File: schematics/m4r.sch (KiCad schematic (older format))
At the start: 88 parts, among them IC10 SN74LVC1G0832, IC11 MAX-M8Q, IC12 NC7SZ04, IC13 CS2100-CP, IC14 Si4463, IC15 NCP380, IC16 Si53307, IC17 BGM1043N7, IC18 ADL5324, IC7 NCP4620, IC8 MCP2562, IC9 STM32F405RxTx, P3 SWD_TC, Y3 TCXO

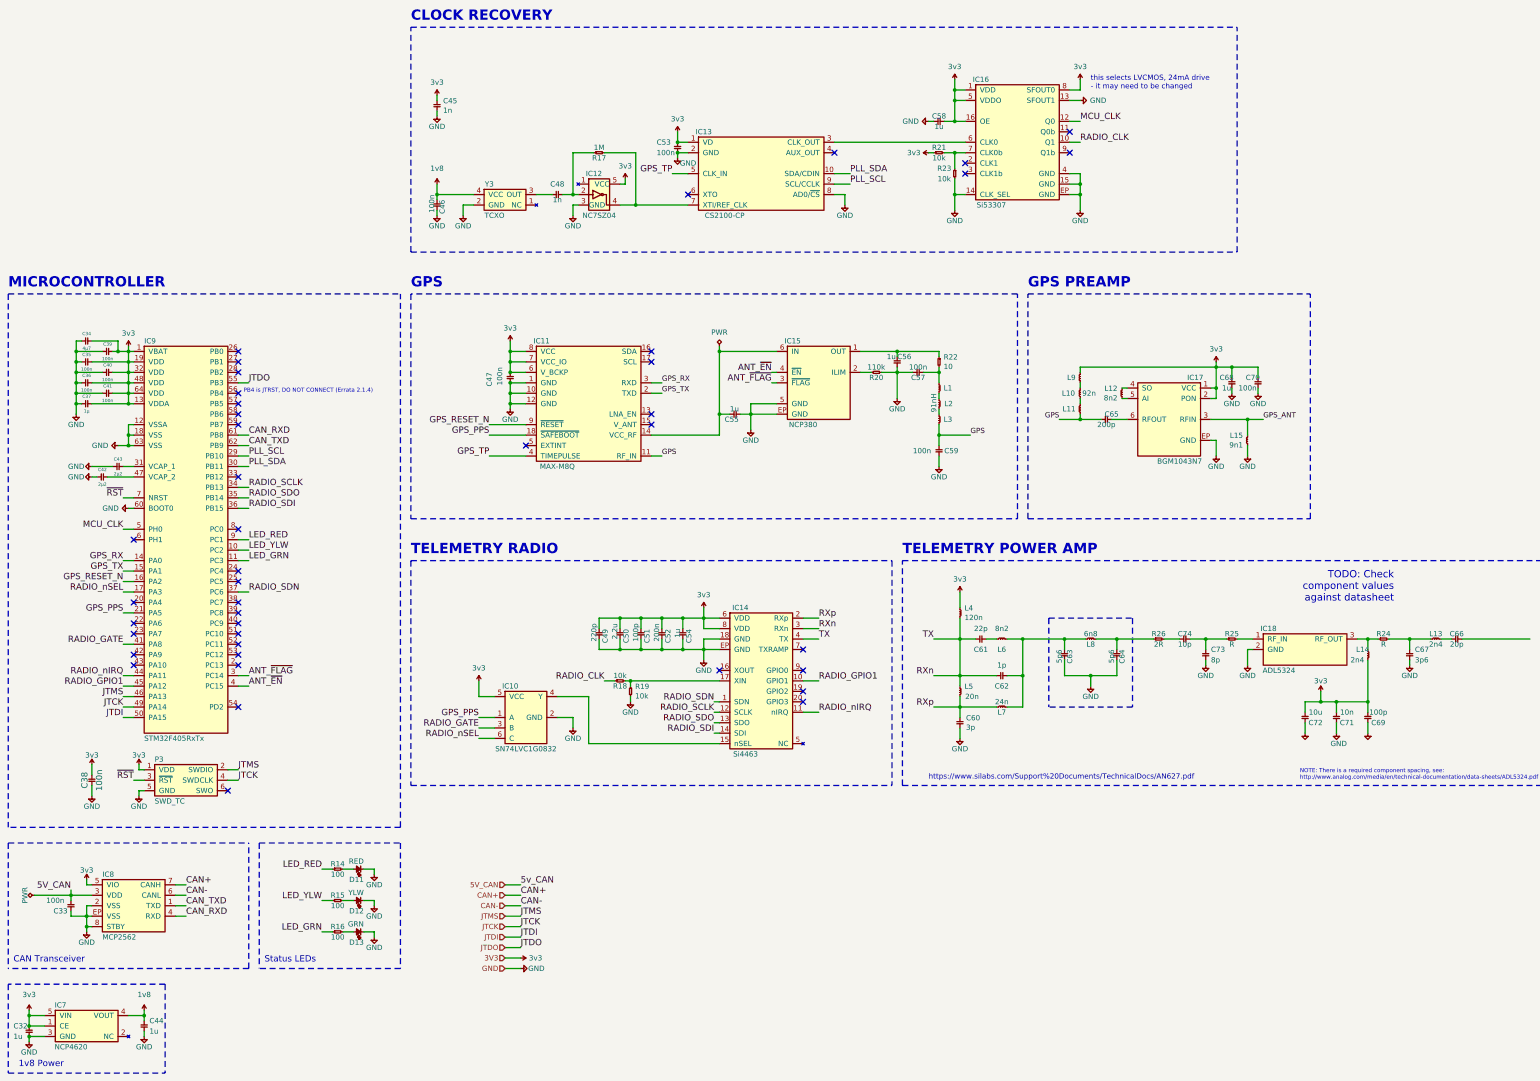
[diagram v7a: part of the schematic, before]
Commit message: Normalise all font sizes to 50 mil
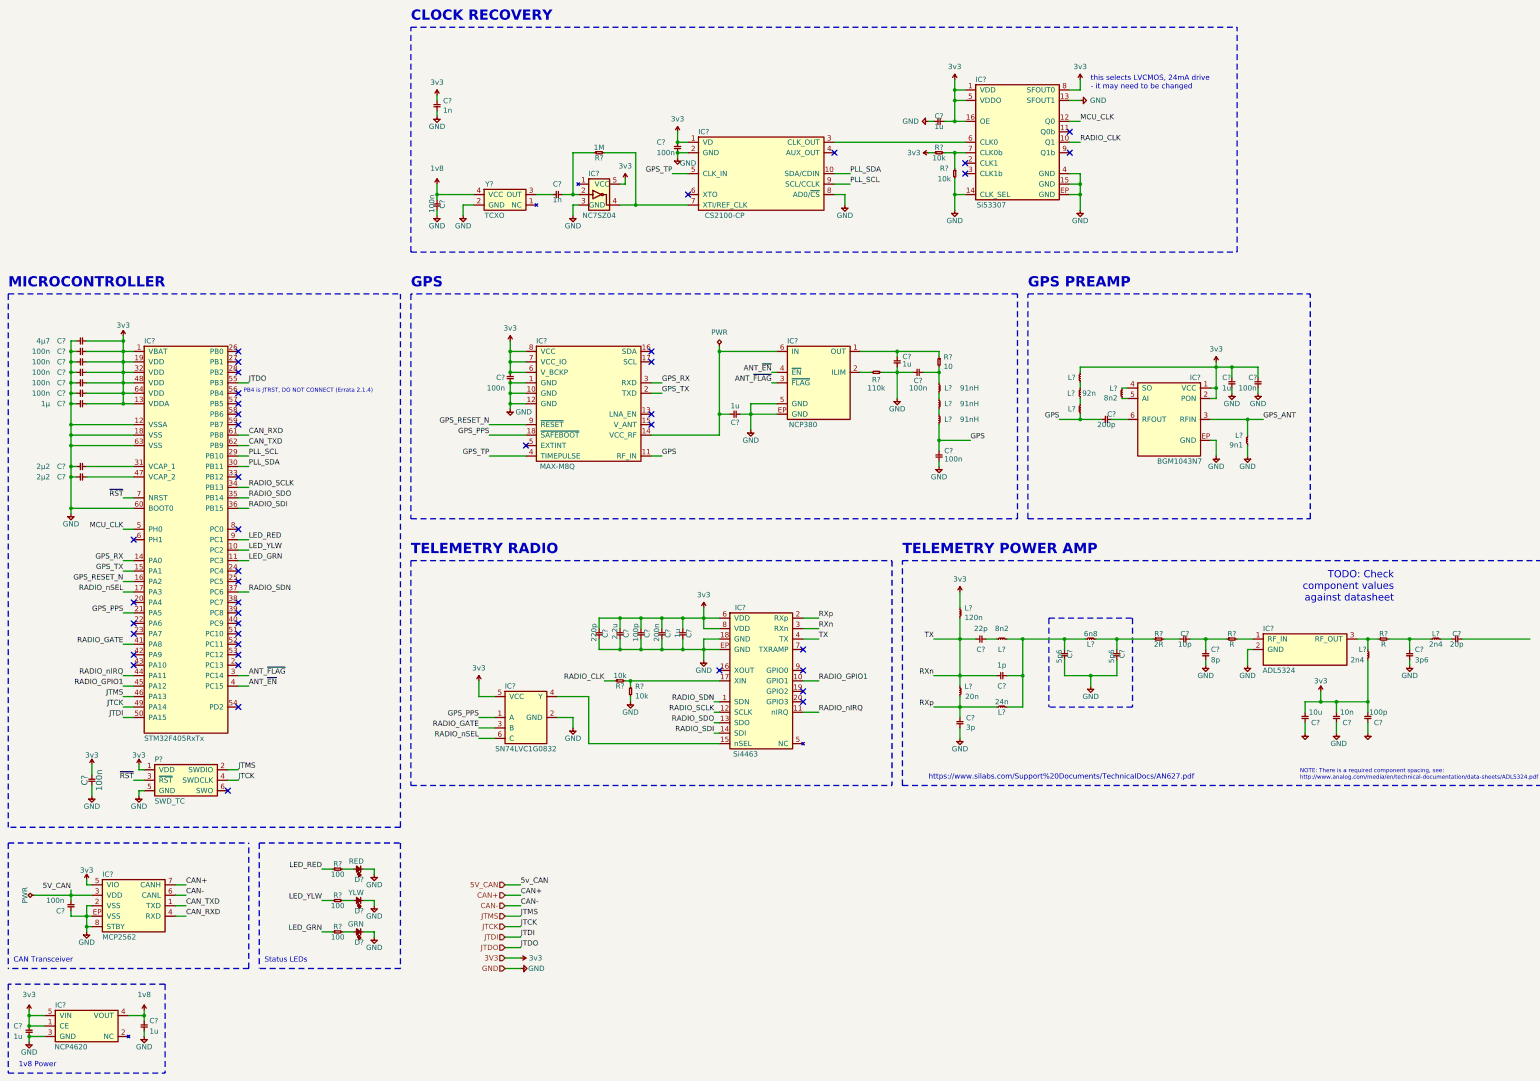
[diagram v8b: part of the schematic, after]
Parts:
- removed C34: 4µ7, agg:0402, symbol cusf-kicad:C
- removed C35, C36, C39, C40, C41: 100n, agg:0402, symbol cusf-kicad:C
- removed C37: 1µ, agg:0402, symbol cusf-kicad:C
- removed C42, C43: 2µ2, agg:0402, symbol cusf-kicad:C
- removed L1, L3: 91nH, symbol cusf-kicad:L
- added C? (x2): 2µ2, agg:0402, symbol cusf-kicad:C
- added C? (x5): 100n, agg:0402, symbol cusf-kicad:C
- added C?: 1µ, agg:0402, symbol cusf-kicad:C
- added C?: 4µ7, agg:0402, symbol cusf-kicad:C
- added L? (x2): 91nH, symbol cusf-kicad:L
- P?: renamed from P3; footprint agg:TC2030-NL -> cusf:TC2030-NL
- renumbered C47 to C?, C46 to C?, C59 to C?, C48 to C?, C55 to C?, C53 to C?, C45 to C?, C56 to C?, C32 to C?, C44 to C?, C54 to C?, C52 to C?, C51 to C?, C50 to C?, C49 to C?, C57 to C?, C73 to C?, C74 to C?, C58 to C?, C68 to C?, C70 to C?, C60 to C?, C67 to C?, C62 to C?, C61 to C?, C65 to C?, C66 to C?, C63 to C?, C64 to C?, C69 to C?, C71 to C?, C72 to C?, C33 to C?, C38 to C?, D11 to D?, D12 to D?, D13 to D?, IC8 to IC?, IC11 to IC?, IC12 to IC?, IC13 to IC?, IC15 to IC?, IC7 to IC?, IC10 to IC?, IC14 to IC?, IC18 to IC?, IC17 to IC?, IC16 to IC?, IC9 to IC?, L2 to L?, L15 to L?, L5 to L?, L7 to L?, L6 to L?, L12 to L?, L13 to L?, L4 to L?, L8 to L?, L14 to L?, L10 to L?, L11 to L?, L9 to L?, R14 to R?, R15 to R?, R17 to R?, R20 to R?, R22 to R?, R18 to R?, R19 to R?, R25 to R?, R26 to R?, R21 to R?, R24 to R?, R23 to R?, R16 to R?, Y3 to Y?
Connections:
- net 3v3: now also C?.2, C?.2, C?.2, C?.2, C?.2, C?.2, C?.2
- net GND: now also C?.1, C?.1, C?.1, C?.1, C?.1, C?.1, C?.1, C?.1, C?.1
- net GPS: now also L?.2
- net at C?.2, R?.2: now also L?.1
- net at L?.1: now also L?.2
- net at L?.2: now also L?.1
- net at IC?.31 (VCAP_1): now also C?.2
- net at IC?.47 (VCAP_2): now also C?.2
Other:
- moved on the sheet: C?
